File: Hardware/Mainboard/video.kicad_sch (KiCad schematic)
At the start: 1 part, among them J9 Conn_02x12_Odd_Even

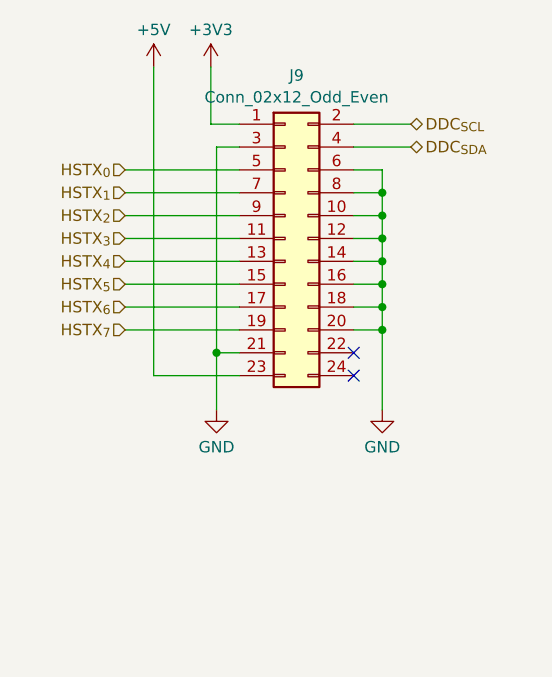
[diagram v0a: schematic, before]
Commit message: Adds more work on the mainboard schematic
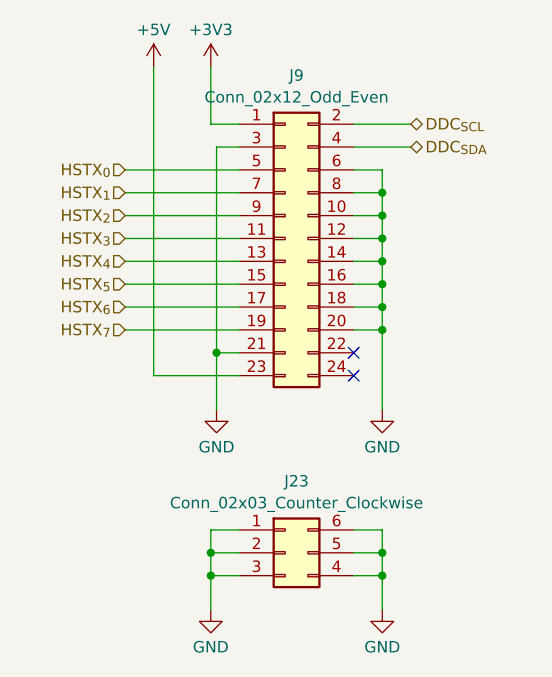
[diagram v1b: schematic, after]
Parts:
- added J23: Conn_02x03_Counter_Clockwise, Connector_PinSocket_2.54mm:PinSocket_2x03_P2.54mm_Vertical, symbol Connector_Generic:Conn_02x03_Counter_Clockwise
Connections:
- net GND: now also J23.1 (Pin_1), J23.2 (Pin_2), J23.3 (Pin_3), J23.4 (Pin_4), J23.5 (Pin_5), J23.6 (Pin_6)
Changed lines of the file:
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@@
 (kicad_sch (version 20230121) (generator eeschema)
   (paper "A4")
+  (junction (at 73.025 88.265) (diameter 0) (color 0 0 0 0)
+  )
   (junction (at 73.025 55.88) (diameter 0) (color 0 0 0 0)
   )
+  (junction (at 73.025 85.725) (diameter 0) (color 0 0 0 0)
+  )
   (junction (at 73.025 60.96) (diameter 0) (color 0 0 0 0)
   )
+  (junction (at 53.975 88.265) (diameter 0) (color 0 0 0 0)
+  )
   (junction (at 73.025 53.34) (diameter 0) (color 0 0 0 0)
   )
@@
   )
   (junction (at 54.61 63.5) (diameter 0) (color 0 0 0 0)
+  )
+  (junction (at 53.975 85.725) (diameter 0) (color 0 0 0 0)
   )
   (junction (at 73.025 45.72) (diameter 0) (color 0 0 0 0)
@@
     (stroke (width 0) (type default))
   )
+  (wire (pts (xy 53.975 85.725) (xy 57.15 85.725))
+    (stroke (width 0) (type default))
+  )
   (wire (pts (xy 73.025 43.18) (xy 73.025 45.72))
     (stroke (width 0) (type default))
@@
     (stroke (width 0) (type default))
   )
+  (wire (pts (xy 69.85 88.265) (xy 73.025 88.265))
+    (stroke (width 0) (type default))
+  )
   (wire (pts (xy 73.025 58.42) (xy 73.025 60.96))
     (stroke (width 0) (type default))
@@
     (stroke (width 0) (type default))
   )
+  (wire (pts (xy 53.975 88.265) (xy 53.975 92.075))
+    (stroke (width 0) (type default))
+  )
+  (wire (pts (xy 73.025 88.265) (xy 73.025 92.075))
+    (stroke (width 0) (type default))
+  )
+  (wire (pts (xy 53.975 88.265) (xy 57.15 88.265))
+    (stroke (width 0) (type default))
+  )
+  (wire (pts (xy 53.975 85.725) (xy 53.975 88.265))
+    (stroke (width 0) (type default))
+  )
+  (wire (pts (xy 73.025 83.185) (xy 73.025 85.725))
+    (stroke (width 0) (type default))
+  )
+  (wire (pts (xy 69.85 85.725) (xy 73.025 85.725))
+    (stroke (width 0) (type default))
+  )
+  (wire (pts (xy 69.85 83.185) (xy 73.025 83.185))
+    (stroke (width 0) (type default))
+  )
   (wire (pts (xy 44.45 55.88) (xy 57.15 55.88))
     (stroke (width 0) (type default))
@@
     (stroke (width 0) (type default))
   )
+  (wire (pts (xy 53.975 83.185) (xy 53.975 85.725))
+    (stroke (width 0) (type default))
+  )
   (wire (pts (xy 54.61 63.5) (xy 54.61 69.85))
+    (stroke (width 0) (type default))
+  )
+  (wire (pts (xy 57.15 83.185) (xy 53.975 83.185))
+    (stroke (width 0) (type default))
+  )
+  (wire (pts (xy 73.025 85.725) (xy 73.025 88.265))
     (stroke (width 0) (type default))
   )
@@
   (hierarchical_label "HSTX_{1}" (shape input) (at 44.45 45.72 180) (fields_autoplaced)
     (effects (font (size 1.27 1.27)) (justify right))
+  )
+  (symbol (lib_id "power:GND") (at 53.975 92.075 0) (unit 1)
+    (in_bom yes) (on_board yes) (dnp no) (fields_autoplaced)
+    (property "Reference" "#PWR0109" (at 53.975 98.425 0)
+      (effects (font (size 1.27 1.27)) hide)
+    )
+    (property "Value" "GND" (at 53.975 96.2081 0)
+      (effects (font (size 1.27 1.27)))
+    )
+    (property "Footprint" "" (at 53.975 92.075 0)
+      (effects (font (size 1.27 1.27)) hide)
+    )
+    (property "Datasheet" "" (at 53.975 92.075 0)
+      (effects (font (size 1.27 1.27)) hide)
+    )
+    (pin "1")
+    (instances
+      (project "Mainboard"
+        (path "/e63e39d7-6ac0-4ffd-8aa3-1841a4541b55/aac41a65-dc0c-4785-ad7d-110c8781d14b"
+          (reference "#PWR0109") (unit 1)
+        )
+      )
+    )
   )
   (symbol (lib_id "Connector_Generic:Conn_02x12_Odd_Even") (at 62.23 50.8 0) (unit 1)
@@
     )
   )
+  (symbol (lib_id "Connector_Generic:Conn_02x03_Counter_Clockwise") (at 62.23 85.725 0) (unit 1)
+    (in_bom yes) (on_board yes) (dnp no) (fields_autoplaced)
+    (property "Reference" "J23" (at 63.5 77.7707 0)
+      (effects (font (size 1.27 1.27)))
+    )
+    (property "Value" "Conn_02x03_Counter_Clockwise" (at 63.5 80.1949 0)
+      (effects (font (size 1.27 1.27)))
+    )
+    (property "Footprint" "Connector_PinSocket_2.54mm:PinSocket_2x03_P2.54mm_Vertical" (at 62.23 85.725 0)
+      (effects (font (size 1.27 1.27)) hide)
+    )
+    (property "Datasheet" "~" (at 62.23 85.725 0)
+      (effects (font (size 1.27 1.27)) hide)
+    )
+    (pin "2")
+    (pin "5")
+    (pin "3")
+    (pin "1")
+    (pin "4")
+    (pin "6")
+    (instances
+      (project "Mainboard"
+        (path "/e63e39d7-6ac0-4ffd-8aa3-1841a4541b55/aac41a65-dc0c-4785-ad7d-110c8781d14b"
+          (reference "J23") (unit 1)
+        )
+      )
+    )
+  )
   (symbol (lib_id "power:GND") (at 73.025 69.85 0) (unit 1)
     (in_bom yes) (on_board yes) (dnp no) (fields_autoplaced)
@@
         )
       )
+    )
+  )
+  (symbol (lib_id "power:GND") (at 73.025 92.075 0) (unit 1)
+    (in_bom yes) (on_board yes) (dnp no) (fields_autoplaced)
+    (property "Reference" "#PWR0110" (at 73.025 98.425 0)
+      (effects (font (size 1.27 1.27)) hide)
+    )
+    (property "Value" "GND" (at 73.025 96.2081 0)
+      (effects (font (size 1.27 1.27)))
+    )
+    (property "Footprint" "" (at 73.025 92.075 0)
+      (effects (font (size 1.27 1.27)) hide)
+    )
+    (property "Datasheet" "" (at 73.025 92.075 0)
+      (effects (font (size 1.27 1.27)) hide)
+    )
+    (pin "1")
+    (instances
+      (project "Mainboard"
+        (path "/e63e39d7-6ac0-4ffd-8aa3-1841a4541b55/aac41a65-dc0c-4785-ad7d-110c8781d14b"
+          (reference "#PWR0110") (unit 1)
+        )
+      )

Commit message: More work on the motherboard
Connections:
- net DDC_{SCL}: now also J9.4 (Pin_4); no longer J9.2 (Pin_2)
- net DDC_{SDA}: now also J9.2 (Pin_2); no longer J9.4 (Pin_4)
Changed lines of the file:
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@@
 	(hierarchical_label "DDC_{SCL}"
 		(shape bidirectional)
-		(at 76.2 38.1 0)
+		(at 76.2 40.64 0)
 		(fields_autoplaced yes)
 		(effects
@@
 	(hierarchical_label "DDC_{SDA}"
 		(shape bidirectional)
-		(at 76.2 40.64 0)
+		(at 76.2 38.1 0)
 		(fields_autoplaced yes)
 		(effects
